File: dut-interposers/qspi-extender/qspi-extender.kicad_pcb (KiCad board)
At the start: 2 copper layers, 104.5 x 6.5 mm, 4 parts, among them J1 103P010BB1100, J2 103R010BB100, M2 MECHANICAL, M3 MECHANICAL

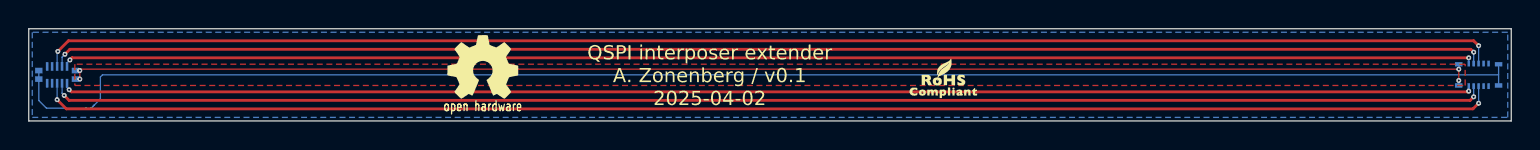
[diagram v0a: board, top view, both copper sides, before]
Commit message: qspi-extender: v0.3 with thinner tracks
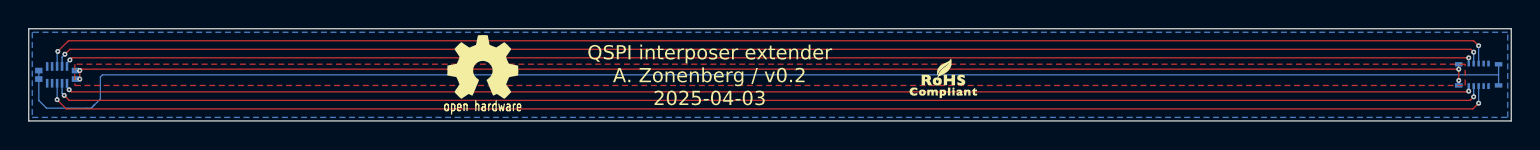
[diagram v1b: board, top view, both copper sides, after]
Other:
- board text added: "QSPI interposer extender A. Zonenberg / v0.2 2025-04-03"
- board text removed: "QSPI interposer extender A. Zonenberg / v0.1 2025-04-02"
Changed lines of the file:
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@@
 		(layer "User.1")
 	)
-	(gr_text "QSPI interposer extender\nA. Zonenberg / v0.1\n2025-04-02"
+	(gr_text "QSPI interposer extender\nA. Zonenberg / v0.2\n2025-04-03"
 		(at 90 104.25 0)
 		(layer "F.SilkS")
@@
 		(start 143.45 103.2)
 		(end 45 103.2)
-		(width 0.2)
+		(width 0.075)
 		(layer "F.Cu")
 		(net 2)
@@
 		(start 143.5 103.15)
 		(end 143.45 103.2)
-		(width 0.2)
+		(width 0.075)
 		(layer "F.Cu")
 		(net 2)
@@
 		(start 45 103.2)
 		(end 44.85 103.05)
-		(width 0.2)
+		(width 0.075)
 		(layer "F.Cu")
 		(net 2)
@@
 		(start 143.8 104.4)
 		(end 44.65 104.4)
-		(width 0.2)
+		(width 0.075)
 		(layer "F.Cu")
 		(net 3)
@@
 		(start 144.2 104)
 		(end 143.8 104.4)
-		(width 0.2)
+		(width 0.075)
 		(layer "F.Cu")
 		(net 3)
@@
 		(start 44.65 104.4)
 		(end 44 103.75)
-		(width 0.2)
+		(width 0.075)
 		(layer "F.Cu")
 		(net 3)
@@
 		(start 143.6 103.8)
 		(end 44.85 103.8)
-		(width 0.2)
+		(width 0.075)
 		(layer "F.Cu")
 		(net 5)
@@
 		(start 44.85 103.8)
 		(end 44.5 103.45)
-		(width 0.2)
+		(width 0.075)
 		(layer "F.Cu")
 		(net 5)
@@
 		(start 143.85 103.55)
 		(end 143.6 103.8)
-		(width 0.2)
+		(width 0.075)
 		(layer "F.Cu")
 		(net 5)
@@
 		(start 44.9 100.2)
 		(end 44.55 100.55)
-		(width 0.2)
+		(width 0.075)
 		(layer "F.Cu")
 		(net 8)
@@
 		(start 143.85 100.4)
 		(end 143.65 100.2)
-		(width 0.2)
+		(width 0.075)
 		(layer "F.Cu")
 		(net 8)
@@
 		(start 143.65 100.2)
 		(end 44.9 100.2)
-		(width 0.2)
+		(width 0.075)
 		(layer "F.Cu")
 		(net 8)
@@
 		(start 44.8 99.6)
 		(end 44.05 100.35)
-		(width 0.2)
+		(width 0.075)
 		(layer "F.Cu")
 		(net 10)
@@
 		(start 143.85 99.6)
 		(end 44.8 99.6)
-		(width 0.2)
+		(width 0.075)
 		(layer "F.Cu")
 		(net 10)
@@
 		(start 144.2 99.95)
 		(end 143.85 99.6)
-		(width 0.2)
+		(width 0.075)
 		(layer "F.Cu")
 		(net 10)
@@
 		(start 45.05 100.8)
 		(end 44.9 100.95)
-		(width 0.2)
+		(width 0.075)
 		(layer "F.Cu")
 		(net 11)
@@
 		(start 143.5 100.8)
 		(end 45.05 100.8)
-		(width 0.2)
+		(width 0.075)
 		(layer "F.Cu")
 		(net 11)
